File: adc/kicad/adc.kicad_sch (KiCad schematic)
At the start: 98 parts, among them J1 Conn_01x02_Pin, J2 Conn_01x02_Pin, J3 Conn_01x02_Pin, J5 Conn_01x04_Pin, J6 pcie_98, U1 ADS1261B, U2 ESD5344D-TP, U3 TPS7A2050PDBVR, U4 TPS7A2025PDBVR, U6 TPS65135, U7 ADP7182AUJZ-5.0, U8 ADP7182AUJZ-2.5, U9 XC6206P332MR

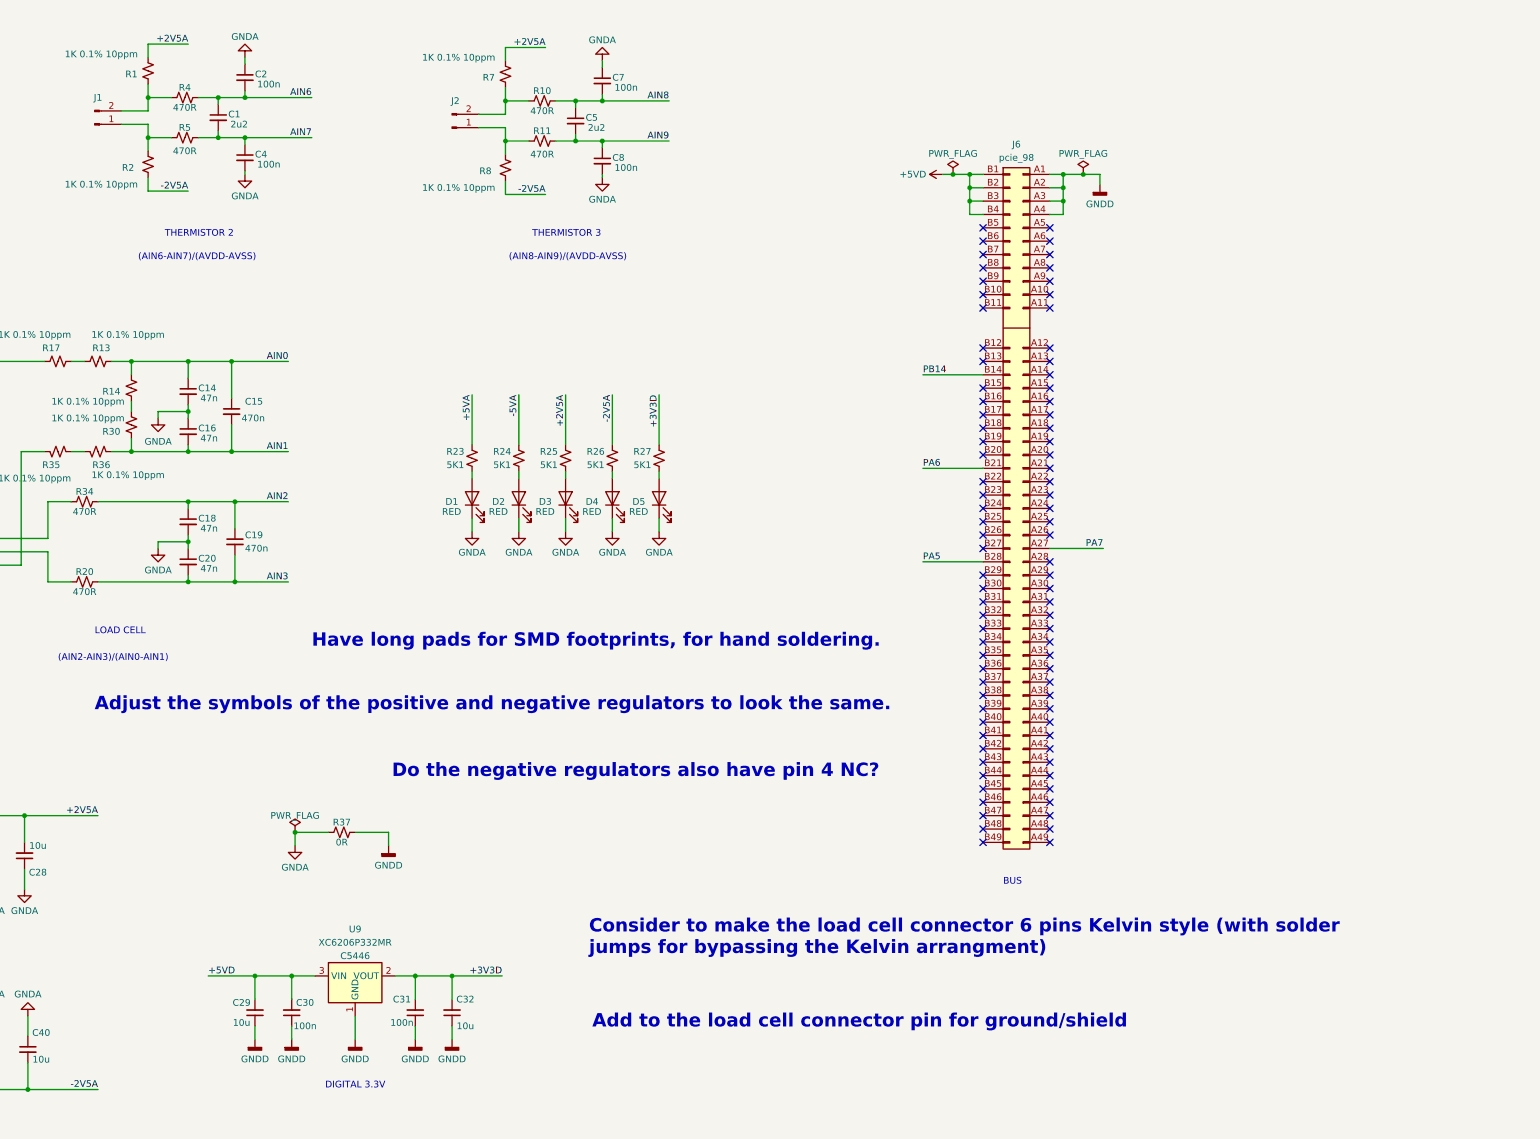
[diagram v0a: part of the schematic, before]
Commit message: Added a comment to the ADC schematic.
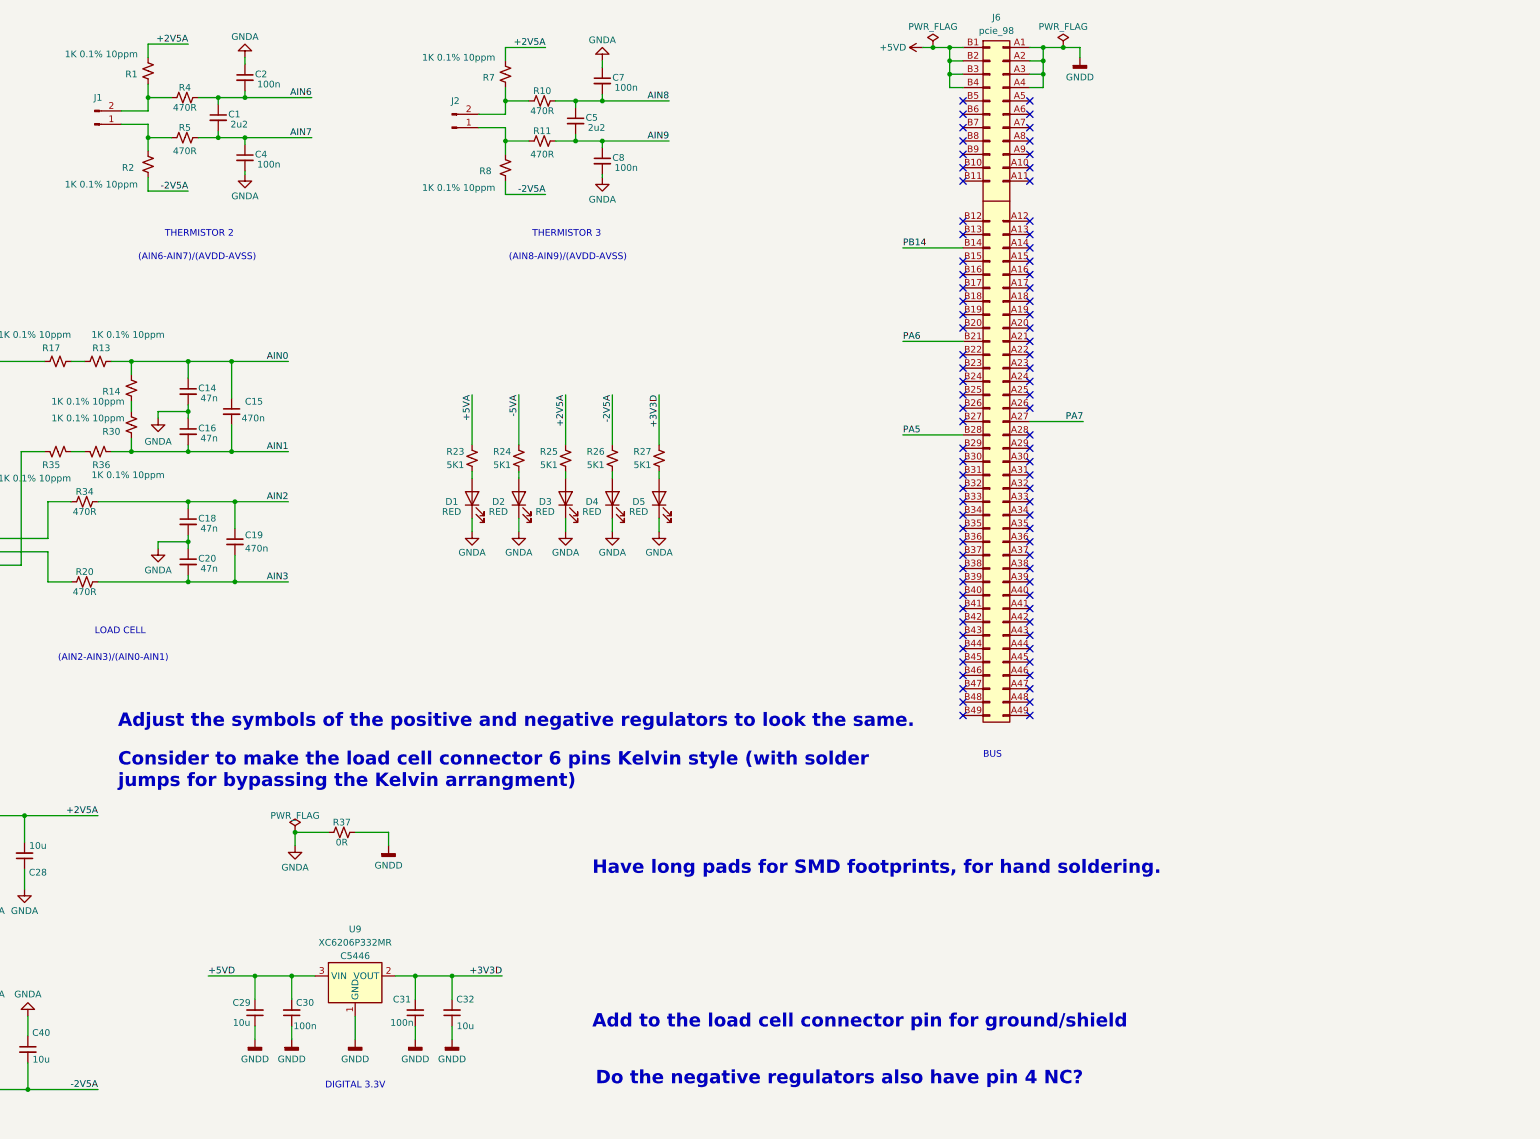
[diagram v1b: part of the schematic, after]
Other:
- moved on the sheet: J6

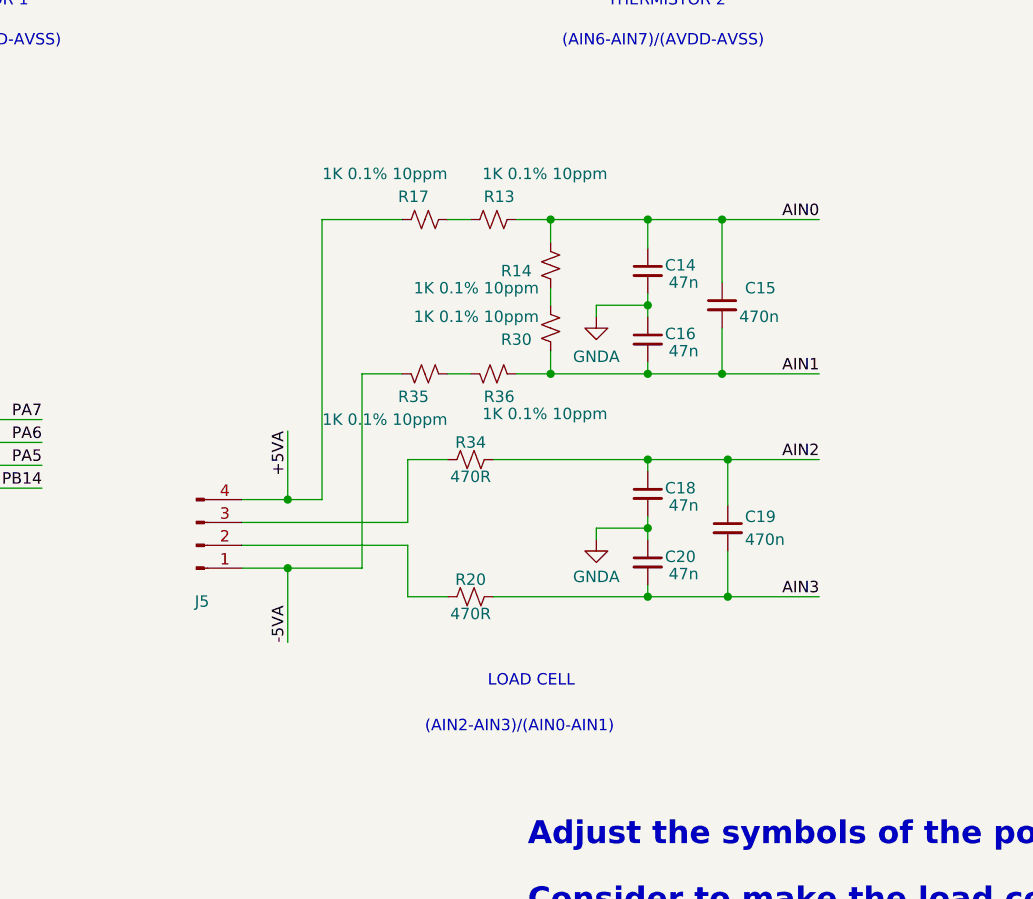
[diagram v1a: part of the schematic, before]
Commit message: Updated the ADC schematic with the new input RC values.
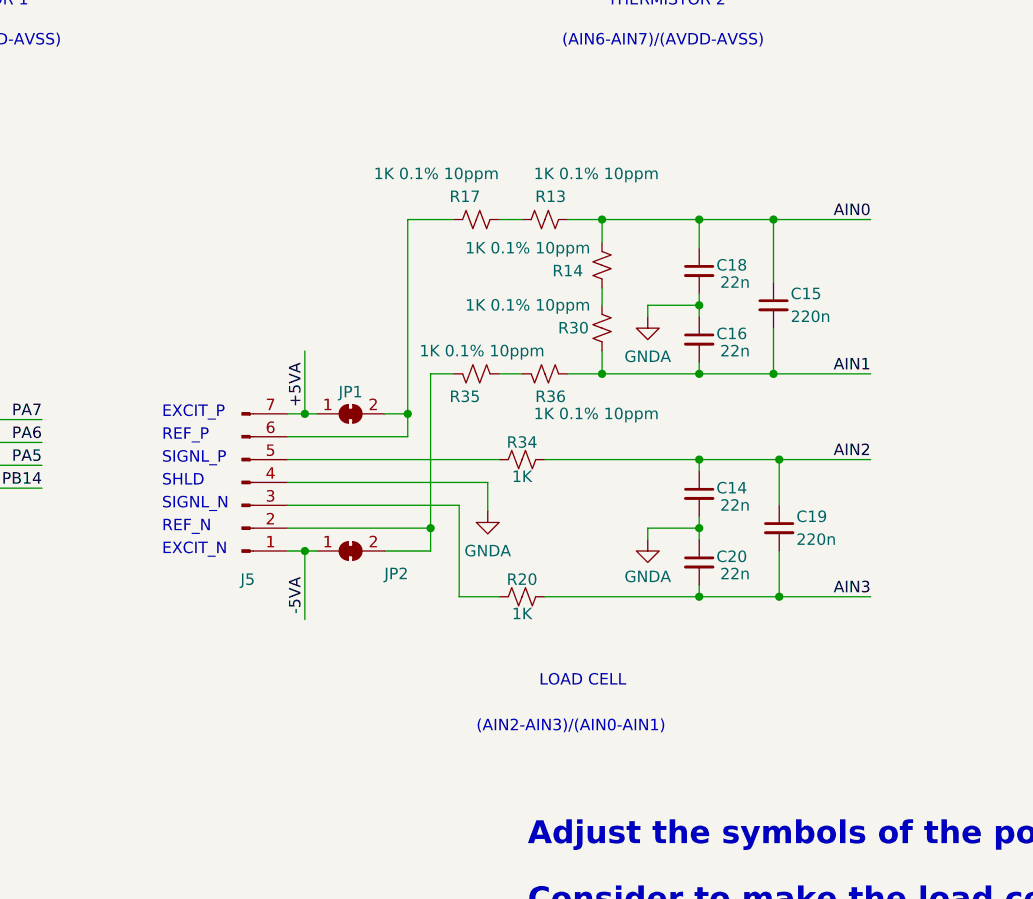
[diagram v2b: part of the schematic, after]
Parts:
- added JP1, JP2: SolderJumper_2_Bridged, symbol Jumper:SolderJumper_2_Bridged
- C14, C16, C18, C20: value 47n -> 22n; LCSC C327054 -> C1532
- C15, C19: value 470n -> 220n; LCSC C47339 -> C16772
- J5: symbol Connector:Conn_01x04_Pin -> Connector:Conn_01x07_Pin
- R20, R34: value 470R -> 1K; LCSC C25117 -> (none)
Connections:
- net +5VA: now also J5.7 (Pin_7), JP1.1 (A); no longer J5.4 (Pin_4), R17.2
- net -5VA: now also JP2.1 (A); no longer R35.2
- net AIN0: now also C18.1; no longer C14.1
- net AIN2: now also C14.1; no longer C18.1
- net GNDA: now also J5.4 (Pin_4)
- net at J5.2 (Pin_2): now also R35.2, JP2.2 (B); no longer R20.1
- net at J5.3 (Pin_3): now also R20.1; no longer R34.1
- new net: J5.6 (Pin_6), JP1.2 (B), R17.2
- new net: J5.5 (Pin_5), R34.1
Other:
- note added: "EXCIT_N"
- note added: "EXCIT_P"
- note added: "REF_N"
- note added: "REF_P"
- note added: "SHLD"
- note added: "SIGNL_N"
- note added: "SIGNL_P"
- moved on the sheet: C19, C20, R13, R14, R17, R20, R30, R34, R35, R36

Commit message: Progressing on the ADC layout.
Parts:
- J1, J2, J3: footprint (none) -> adc:connector_2pins_horizontal; LCSC (none) -> DNP
- J5: value Conn_01x04_Pin -> Conn_01x07_Pin; footprint (none) -> adc:connector_7pins_horizontal; LCSC (none) -> DNP
- J6: LCSC (none) -> DNP
- JP1, JP2: footprint (none) -> Jumper:SolderJumper-2_P1.3mm_Bridged_Pad1.0x1.5mm; LCSC (none) -> DNP
- R20, R34: LCSC (none) -> C11702
- U6: footprint (none) -> Package_DFN_QFN:WQFN-16-1EP_3x3mm_P0.5mm_EP1.68x1.68mm_ThermalVias
- U7: symbol Regulator_Linear:ADP7182AUJZ-5.0 -> adc:ADP7182AUJZ
- U8: symbol Regulator_Linear:ADP7182AUJZ-2.5 -> adc:ADP7182AUJZ
- U9: footprint (none) -> Package_TO_SOT_SMD:SOT-23-3
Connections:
- net GNDA: now also U6.17 (PAD)
- no-connect marks 93 -> 95
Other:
- note added: "TODO: verify footprints against datasheets."
- note added: "TODO: verify pin numbers against datasheets."
- note removed: "Add to the load cell connector pin for ground/shield"
- note removed: "Adjust the symbols of the positive and negative regulators to look the same."
- note removed: "Consider to make the load cell connector 6 pins Kelvin style (with solder jumps for bypassing the Kelvin arrangment)"
- note removed: "Do the negative regulators also have pin 4 NC?"
- moved on the sheet: C1, C14, C15, C16, C18, C19, C2, C20, C23, C24, C25, C26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

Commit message: More progress with the ADC layout.
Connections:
- net PA5: now also U2.5 (D4); no longer U2.2 (D2)
- net PA6: now also U2.2 (D2); no longer U2.4 (D3)
- net PA7: now also U2.4 (D3); no longer U2.5 (D4)
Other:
- moved on the sheet: C1, C2, C29, C30, C31, C32, C4, C5, C7, C8, D1, D2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

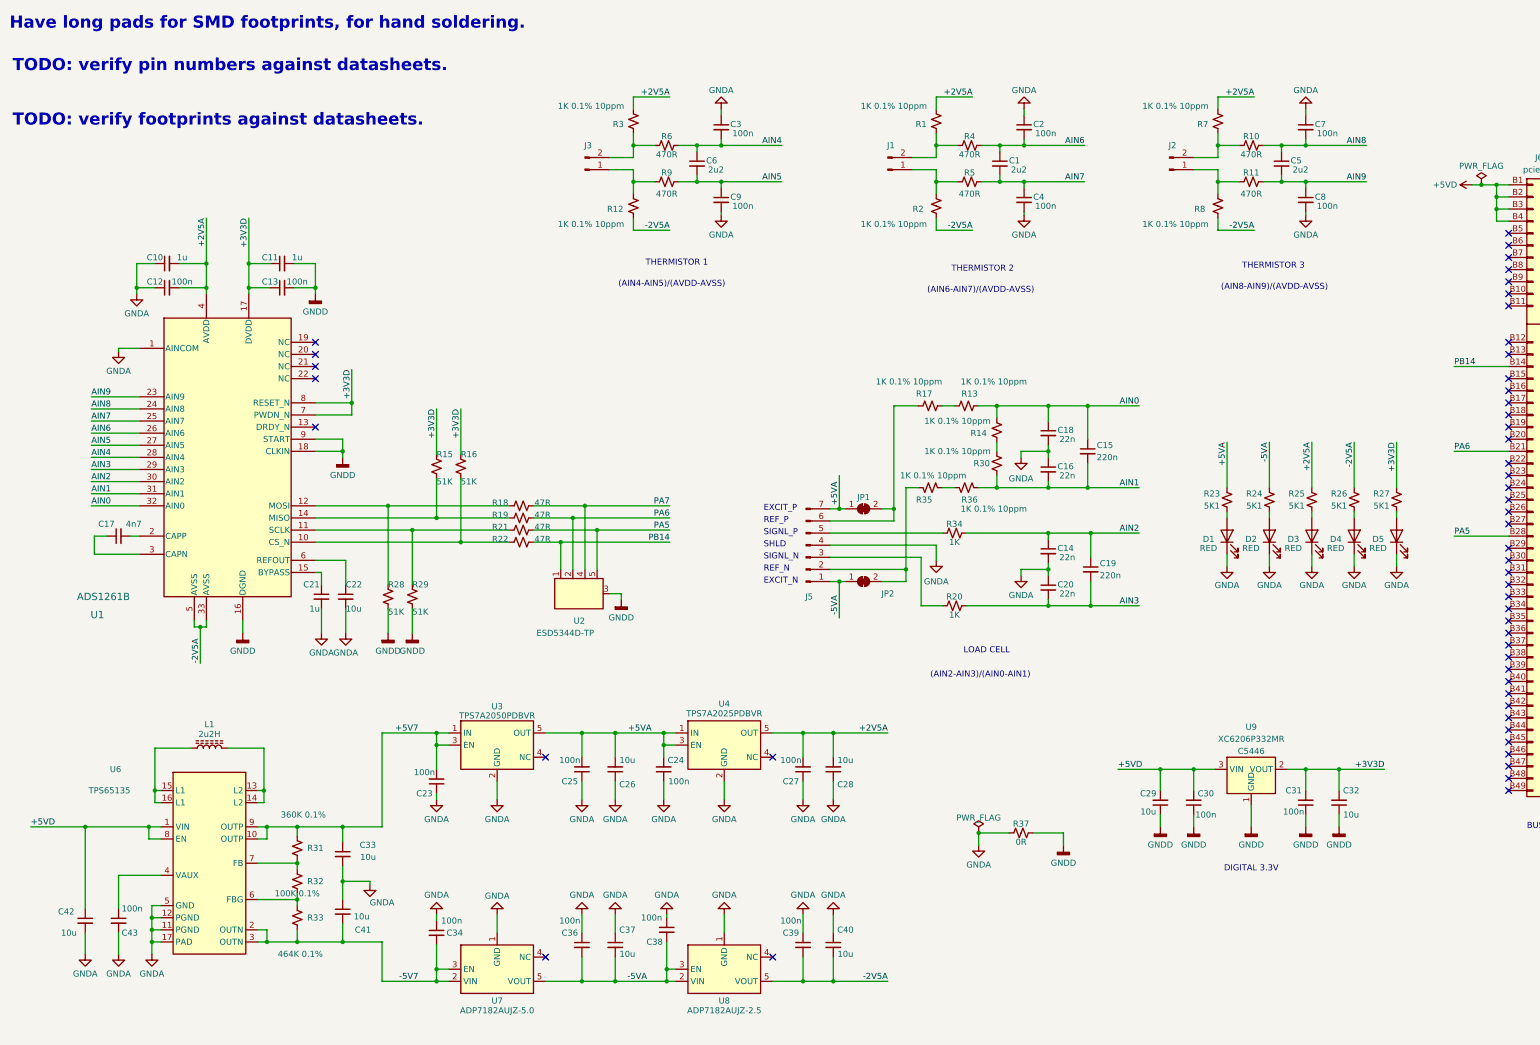
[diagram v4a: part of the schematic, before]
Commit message: Initial topological routing of the ADC board completed.
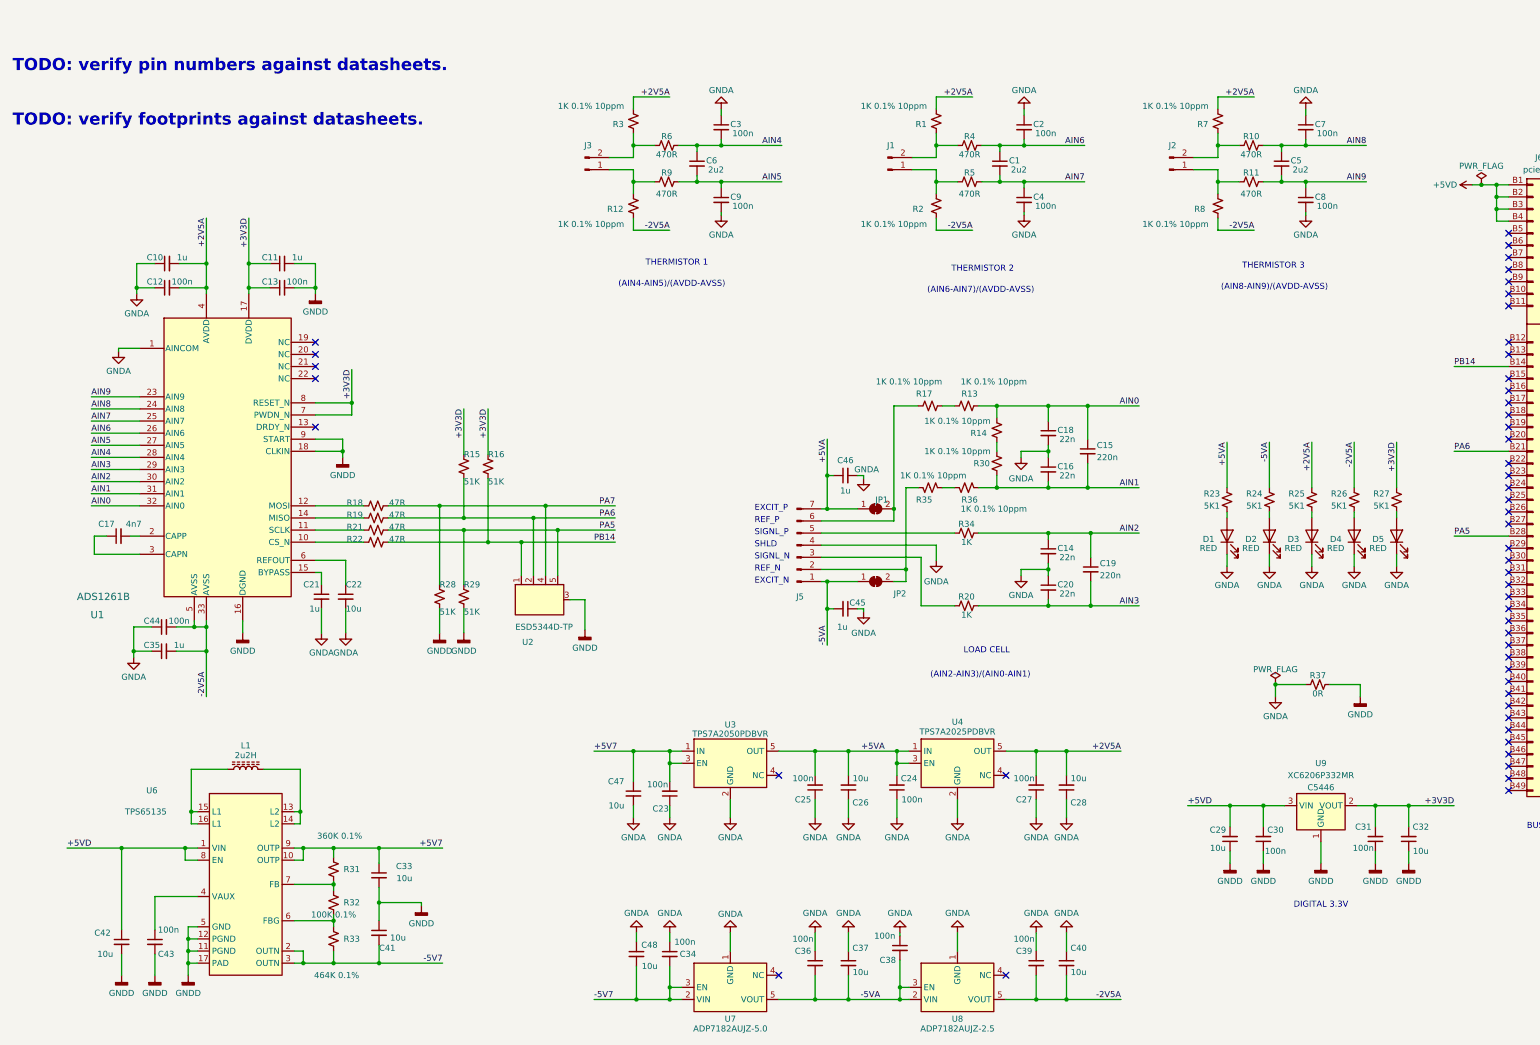
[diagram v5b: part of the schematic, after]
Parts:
- added C35, C45, C46: 1u, Capacitor_SMD:C_0402_1005Metric, symbol Device:C_Small
- added C44: 100n, Capacitor_SMD:C_0402_1005Metric, symbol Device:C_Small
- added C47, C48: 10u, Capacitor_SMD:C_0603_1608Metric, symbol Device:C_Small
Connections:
- net +5V7: now also C47.1
- net +5VA: now also C46.1
- net -2V5A: now also C35.2, C44.2
- net -5V7: now also C48.2
- net -5VA: now also C45.2
- net GNDA: now also C35.1, C44.1, C45.1, C46.2, C47.2, C48.1; no longer C33.2, C41.1, C42.2, C43.2, U6.11 (PGND), U6.12 (PGND), U6.17 (PAD), U6.5 (GND)
- net GNDD: now also C33.2, C41.1, C42.2, C43.2, U6.11 (PGND), U6.12 (PGND), U6.17 (PAD), U6.5 (GND)
- net PA5: now also R29.2
- net PA6: now also R15.1
- net PA7: now also R28.2
- net PB14: now also R16.1
- net at R19.2, U1.14 (MISO): no longer R15.1
- net at R22.2, U1.10 (CS_N): no longer R16.1
- net at R18.2, U1.12 (MOSI): no longer R28.2
- net at R21.2, U1.11 (SCLK): no longer R29.2
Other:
- note removed: "Have long pads for SMD footprints, for hand soldering."
- moved on the sheet: C23, C24, C25, C26, C27, C28, C29, C30, C31, C32, C33, C34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

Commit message: ADC layout is feature complete.
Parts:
- J1, J2, J3: LCSC DNP -> C30436
- J5: LCSC DNP -> C70896
- J6, JP1, JP2: now left out of the parts list
- R10, R11, R4, R5, R6, R9: value 470R -> 1K; LCSC C25117 -> C11702
- U1: value ADS1261B -> ADS1261BIRHBT; LCSC DIGIKEY -> C2669964
- U3: LCSC DIGIKEY -> C2864504
- U4: value TPS7A2025PDBVR -> TPS7A2025PDBVRr; LCSC DIGIKEY -> C2869949
- U7: LCSC DIGIKEY -> C514357
- U8: LCSC DIGIKEY -> C462196
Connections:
- net GNDA: no longer D5.1 (K)
- net GNDD: now also D5.1 (K)
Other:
- note added: "5 CHANNELS DIFFERENTIAL 24BIT ADC"
- note added: "DC/DC +/-5.7V"
- note added: "GROUNDS BRIDGE"
- note added: "INDICATIONS"
- note added: "LOAD CELL INPUT"
- note added: "LOW NOISE LDO +/-5V, +/-2.5V"
- note added: "SPI"
- note removed: "LOAD CELL"
- title: ADS1261 ADC BOARD -> ADS1261B ADC BOARD
- moved on the sheet: C1, C10, C11, C12, C13, C14, C15, C16, C17, C18, C19, C2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
